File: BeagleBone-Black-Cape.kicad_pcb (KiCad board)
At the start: 2 copper layers, 54.6 x 86.4 mm, 2 parts, among them P8 BeagleBone_Black_Header, P9 BeagleBone_Black_Header

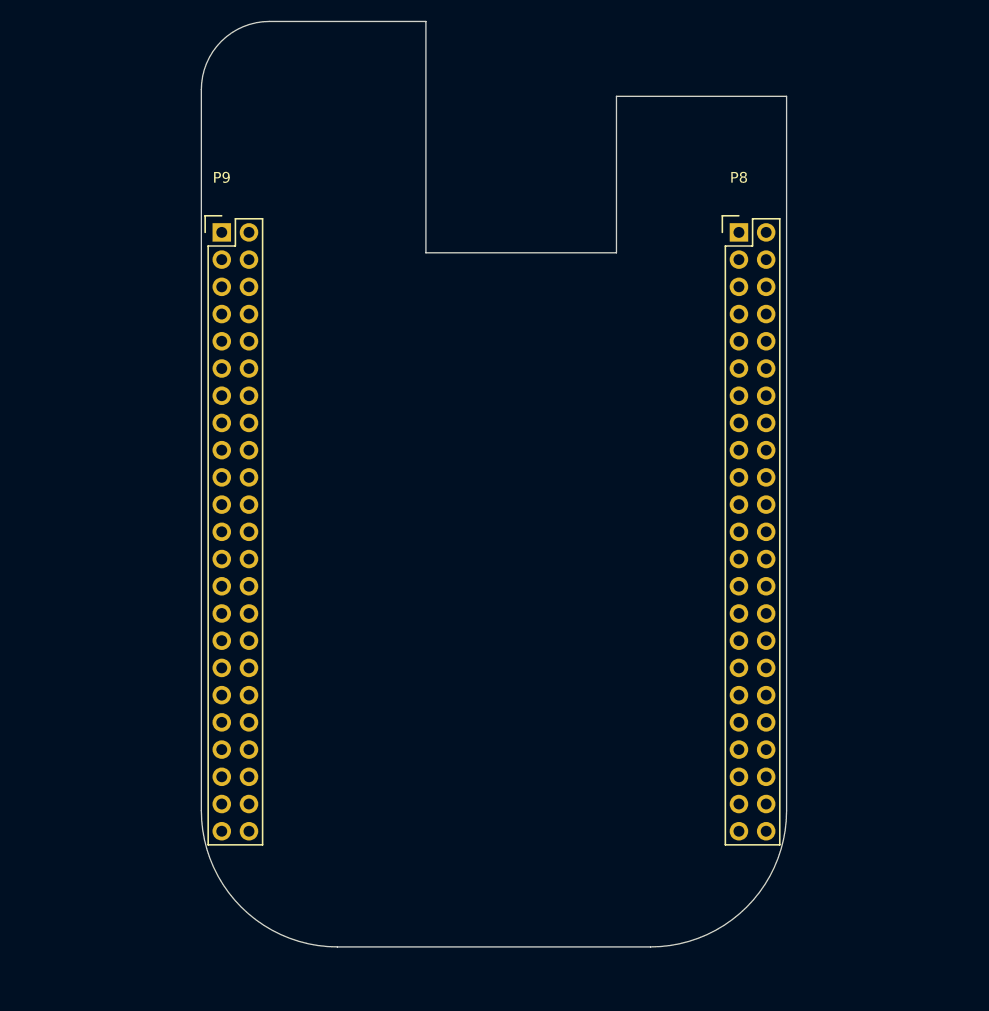
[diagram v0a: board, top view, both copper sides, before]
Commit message: added pad of max5935, started creating pcb
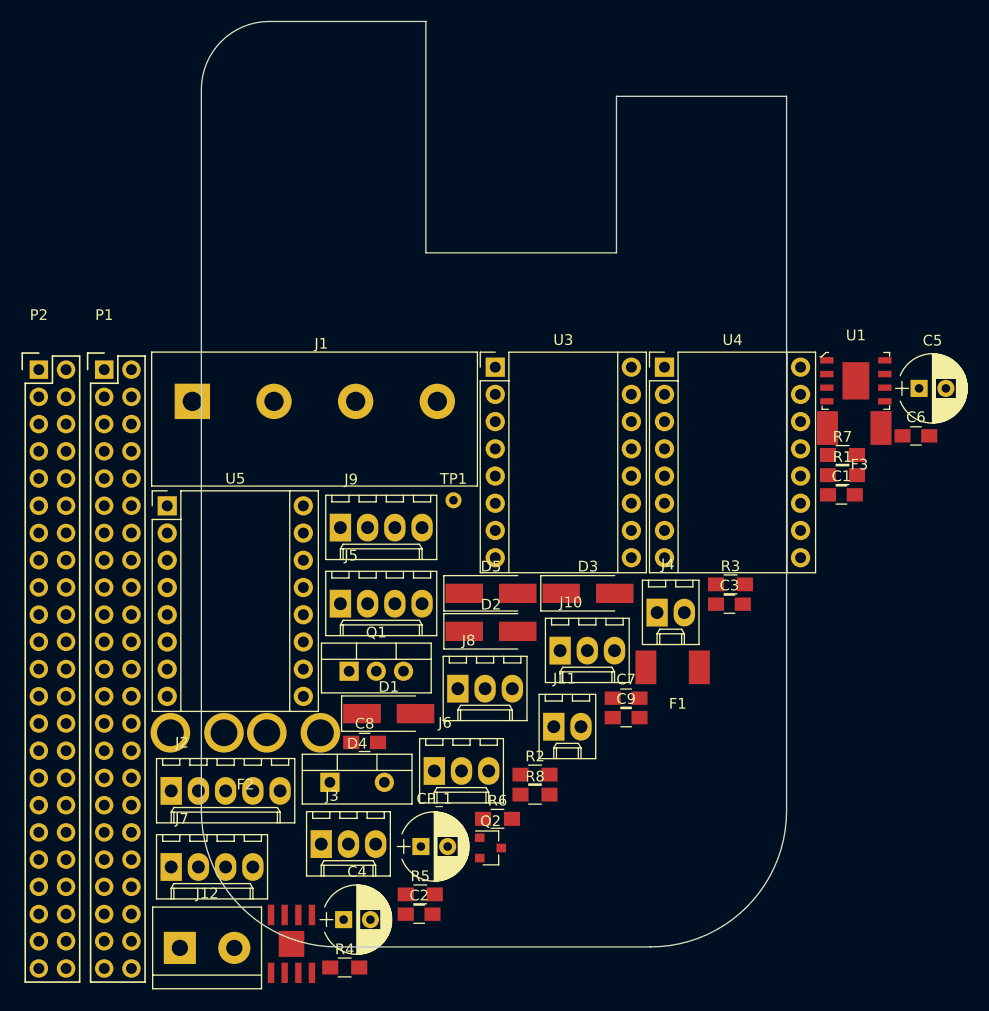
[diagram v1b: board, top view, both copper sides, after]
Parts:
- removed P8, P9: BeagleBone_Black_Header, Socket_BeagleBone_Black:Socket_BeagleBone_Black
- added C1: 47nF, Capacitors_SMD:C_0805_HandSoldering, F.Cu at (174.2, 86.9)
- added C2: 1uF, Capacitors_SMD:C_0805_HandSoldering, F.Cu at (134.8, 126.0)
- added C3: 0.1uF, Capacitors_SMD:C_0805_HandSoldering, F.Cu at (163.7, 97.1)
- added C4: 100uF, Capacitors_THT:CP_Radial_D6.3mm_P2.50mm, F.Cu at (127.7, 126.5)
- added C5: 100uF, Capacitors_THT:CP_Radial_D6.3mm_P2.50mm, F.Cu at (181.4, 76.9)
- added C6: 1uF, Capacitors_SMD:C_0805_HandSoldering, F.Cu at (181.1, 81.4)
- added C7: 0.1uF, Capacitors_SMD:C_0805_HandSoldering, F.Cu at (154.1, 105.8)
- added C8: 0.1uF, Capacitors_SMD:C_0805_HandSoldering, F.Cu at (129.7, 110.0)
- added C9: 0.1uF, Capacitors_SMD:C_0805_HandSoldering, F.Cu at (154.1, 107.7)
- added CP_1: 100uF, Capacitors_THT:CP_Radial_D6.3mm_P2.50mm, F.Cu at (135.0, 119.7)
- added D1: 50V_1A, Diodes_SMD:D_SMA_Handsoldering, F.Cu at (132.0, 107.3)
- added D2: 50V_1A, Diodes_SMD:D_SMA_Handsoldering, F.Cu at (141.5, 99.6)
- added D3: 50V_1A, Diodes_SMD:D_SMA_Handsoldering, F.Cu at (150.5, 96.1)
- added D4: STPS1545D, TO_SOT_Packages_THT:TO-220-2_Vertical, F.Cu at (126.5, 113.7)
- added D5: 50V_1A, Diodes_SMD:D_SMA_Handsoldering, F.Cu at (141.5, 96.1)
- added F1: 2A, Socket_BeagleBone_Black:littlefuse_448, F.Cu at (158.5, 103.0)
- added F2: 30A, Socket_BeagleBone_Black:MCCQ-121, F.Cu at (118.6, 109.1)
- added F3: 4A, Socket_BeagleBone_Black:littlefuse_448, F.Cu at (175.4, 80.6)
- added J1: MC000052, Socket_BeagleBone_Black:MC000052, F.Cu at (113.6, 78.2)
- added J10: MOLEX_2031, Connectors_Molex:Molex_KK-6410-03_03x2.54mm_Straight, F.Cu at (147.9, 101.4)
- added J11: MOLEX_2021, Connectors_Molex:Molex_KK-6410-02_02x2.54mm_Straight, F.Cu at (147.4, 108.5)
- added J12: EBV-02-D, Connectors_Terminal_Blocks:TerminalBlock_bornier-2_P5.08mm, F.Cu at (112.5, 129.1)
- added J2: MOLEX_2051, Connectors_Molex:Molex_KK-6410-05_05x2.54mm_Straight, F.Cu at (111.7, 114.5)
- added J3: MOLEX_2031, Connectors_Molex:Molex_KK-6410-03_03x2.54mm_Straight, F.Cu at (125.7, 119.5)
- added J4: MOLEX_2021, Connectors_Molex:Molex_KK-6410-02_02x2.54mm_Straight, F.Cu at (157.0, 97.9)
- added J5: MOLEX_2041, Connectors_Molex:Molex_KK-6410-04_04x2.54mm_Straight, F.Cu at (127.4, 97.0)
- added J6: MOLEX_2031, Connectors_Molex:Molex_KK-6410-03_03x2.54mm_Straight, F.Cu at (136.2, 112.6)
- added J7: MOLEX_2041, Connectors_Molex:Molex_KK-6410-04_04x2.54mm_Straight, F.Cu at (111.7, 121.6)
- added J8: MOLEX_2031, Connectors_Molex:Molex_KK-6410-03_03x2.54mm_Straight, F.Cu at (138.4, 105.0)
- added J9: MOLEX_2041, Connectors_Molex:Molex_KK-6410-04_04x2.54mm_Straight, F.Cu at (127.4, 89.9)
- added P1: BeagleBone_Black_Header, Socket_BeagleBone_Black:Socket_BeagleBone_Black, F.Cu at (105.4, 75.2)
- added P2: BeagleBone_Black_Header, Socket_BeagleBone_Black:Socket_BeagleBone_Black, F.Cu at (99.3, 75.2)
- added Q1: IRLB8721PBF, TO_SOT_Packages_THT:TO-220-3_Vertical, F.Cu at (128.3, 103.3)
- added Q2: IRFML8244, TO_SOT_Packages_SMD:SOT-23, F.Cu at (141.5, 119.8)
- added R1: 10K, Resistors_SMD:R_0805_HandSoldering, F.Cu at (174.3, 85.0)
- added R2: 10K, Resistors_SMD:R_0805_HandSoldering, F.Cu at (145.6, 113.0)
- added R3: 340K, Resistors_SMD:R_0805_HandSoldering, F.Cu at (163.8, 95.2)
- added R4: 10K, Resistors_SMD:R_0805_HandSoldering, F.Cu at (127.8, 131.0)
- added R5: 10K, Resistors_SMD:R_0805_HandSoldering, F.Cu at (134.9, 124.2)
- added R6: 10K, Resistors_SMD:R_0805_HandSoldering, F.Cu at (142.1, 117.1)
- added R7: 10K, Resistors_SMD:R_0805_HandSoldering, F.Cu at (174.3, 83.2)
- added R8: 10K, Resistors_SMD:R_0805_HandSoldering, F.Cu at (145.6, 114.9)
- added TP1: TestPoint, Measurement_Points:Measurement_Point_Round-TH_Small, F.Cu at (138.0, 87.4)
- added U1: DIGIPOT_50K, Socket_BeagleBone_Black:TDFN-8-1EP, F.Cu at (175.5, 76.2)
- added U2: U_IC-HKB, Socket_BeagleBone_Black:ICHKB, F.Cu at (122.9, 128.8)
- added U3: X_STEPPER, Socket_BeagleBone_Black:TMC2130, F.Cu at (141.9, 75.0)
- added U4: Y_STEPPER, Socket_BeagleBone_Black:TMC2130, F.Cu at (157.7, 75.0)
- added U5: Z_STEPPER, Socket_BeagleBone_Black:TMC2130, F.Cu at (111.3, 87.9)
